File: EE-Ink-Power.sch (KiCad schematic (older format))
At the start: 64 parts, among them J2 USB_A, Q1 IRLML6402, Q2 IRLML6402, Q3 IRLML6402, U4 LM358, U6 MCP73831, U7 MCP1802, U8 LT1945, U9 LT1945

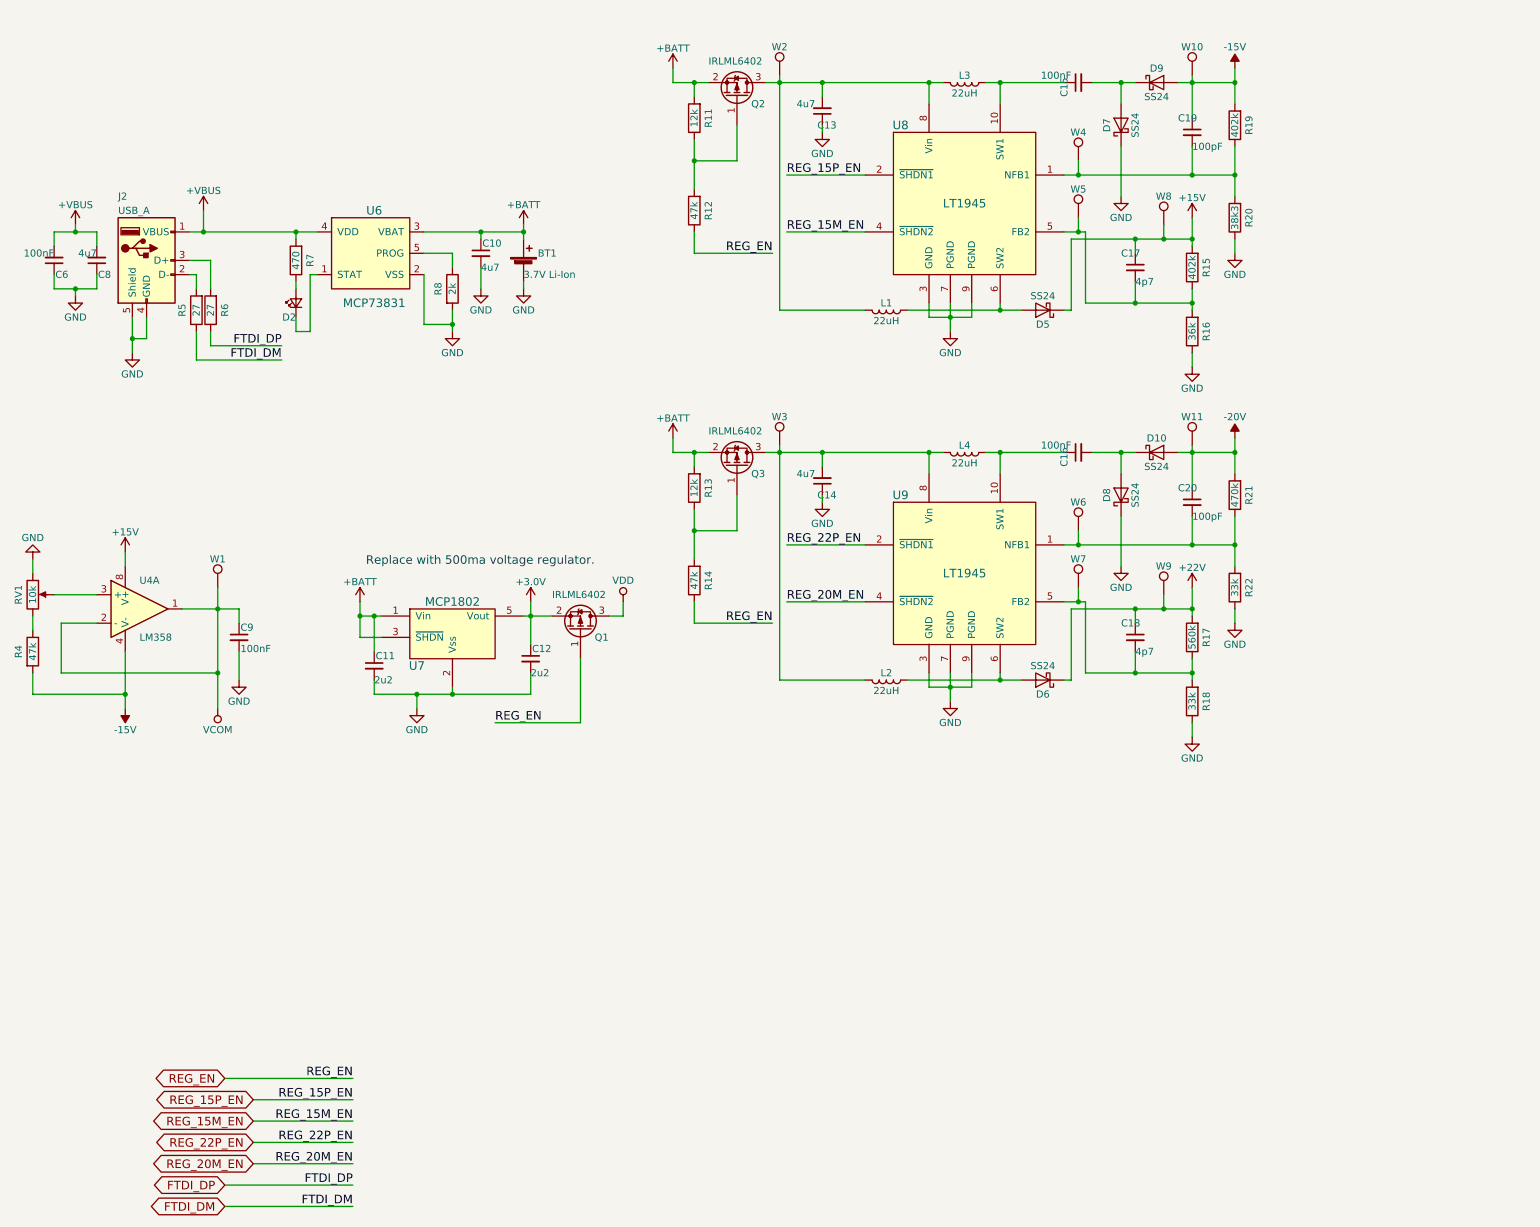
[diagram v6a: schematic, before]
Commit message: Switched out the regulator for a 500ma one.  Cleaned up a few things.
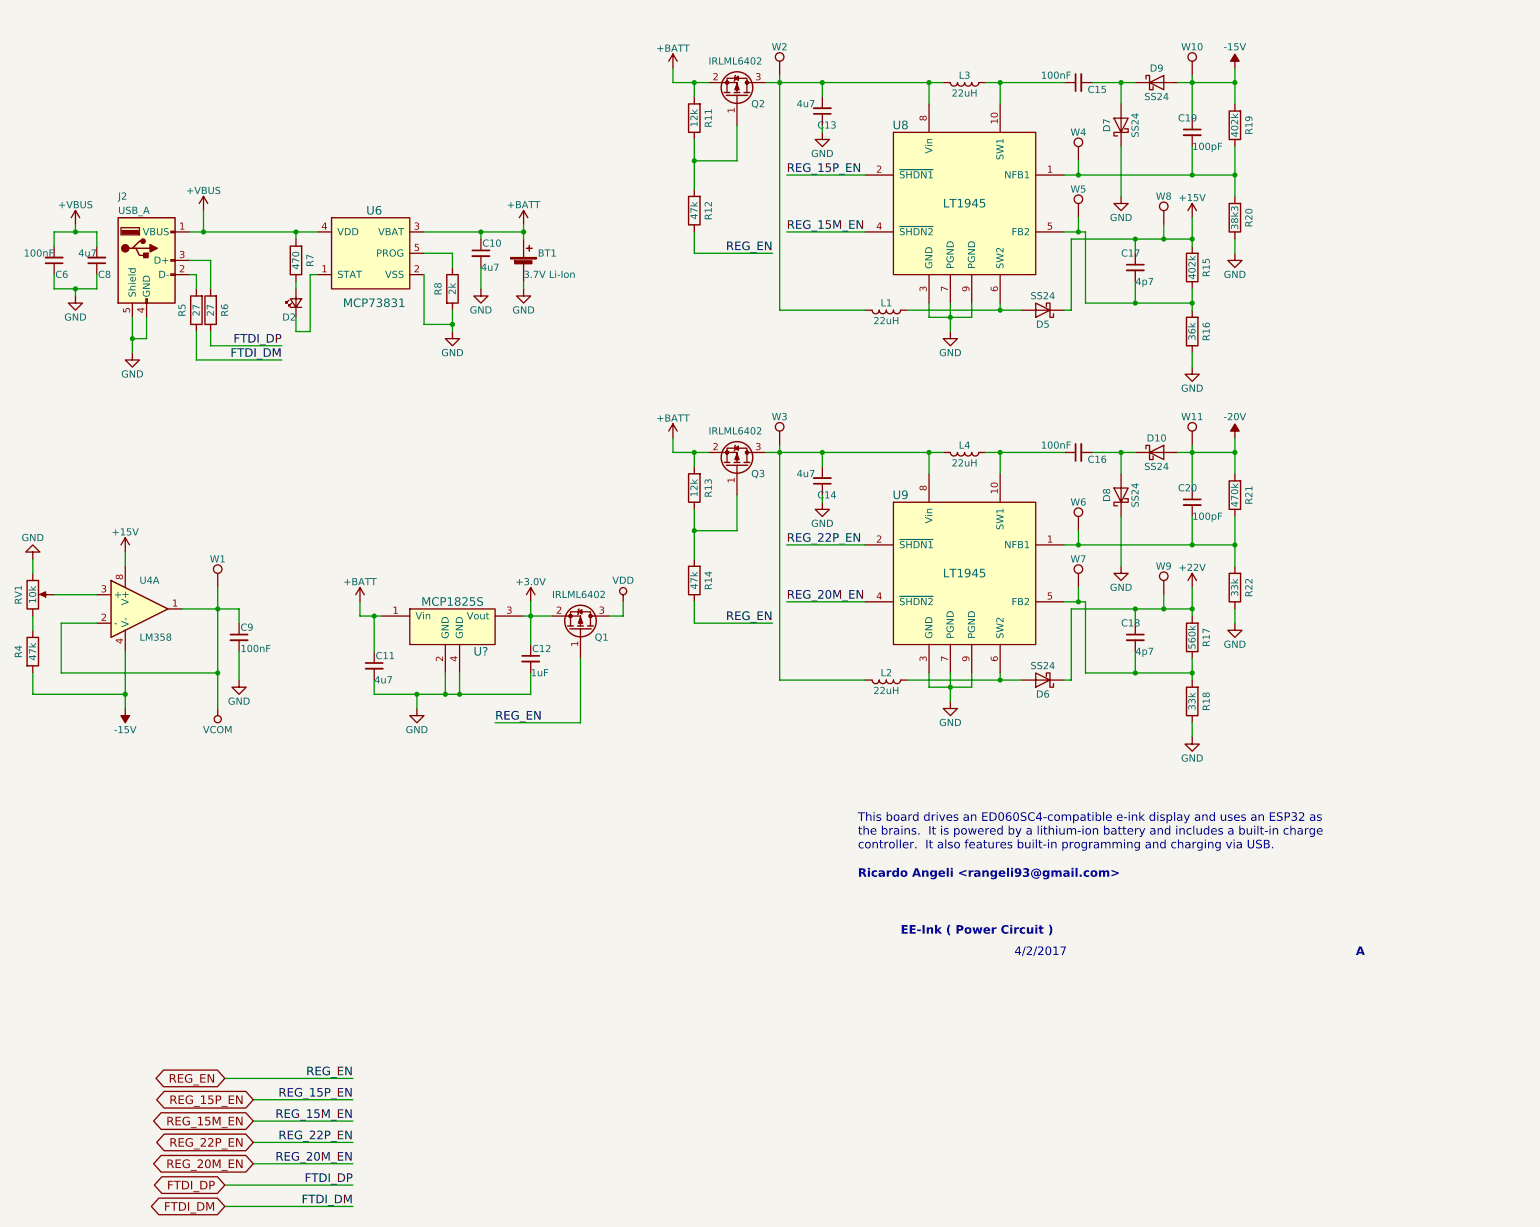
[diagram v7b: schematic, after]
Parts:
- removed U7: MCP1802, symbol MCP1802
- added U?: MCP1825S, symbol MCP1825S
- C11: value 2u2 -> 4u7
- C12: value 2u2 -> 1uF
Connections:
- net +3.0V: now also U?.3 (Vout)
- net +BATT: now also U?.1 (Vin)
- net GND: now also U?.2 (GND), U?.4 (GND)
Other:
- note added: "4/2/2017"
- note added: "A"
- note added: "EE-Ink ( Power Circuit )"
- note added: "Ricardo Angeli <rangeli93@gmail.com>"
- note added: "This board drives an ED060SC4-compatible e-ink display and uses an ESP32 as\nthe brains. It is powered by a lithium-ion battery and includes a built-in charge\ncontroller. It also features built-in programming and charging via USB."
- note removed: "Replace with 500ma voltage regulator."
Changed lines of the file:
@@
 U 1 1 58F29CEA
 P 8600 1500
-F 0 "C15" H 8500 1600 50  0000 L CNN
+F 0 "C15" V 8550 1300 50  0000 L CNN
 F 1 "100nF" V 8650 1550 50  0000 L CNN
 F 2 "" H 8600 1500 50  0001 C CNN
@@
 U 1 1 58F29DC6
 P 8600 4100
-F 0 "C16" H 8500 4200 50  0000 L CNN
+F 0 "C16" V 8550 3900 50  0000 L CNN
 F 1 "100nF" V 8650 4150 50  0000 L CNN
 F 2 "" H 8600 4100 50  0001 C CNN
@@
 $EndComp
 $Comp
-L MCP1802 U7
-U 1 1 58F2D150
-P 4200 5350
-F 0 "U7" H 3950 5100 60  0000 C CNN
-F 1 "MCP1802" H 4200 5550 60  0000 C CNN
-F 2 "" H 4200 5650 60  0001 C CNN
-F 3 "" H 4200 5650 60  0001 C CNN
-	1    4200 5350
-	1    0    0    -1
-$EndComp
-$Comp
 L C_Small C11
 U 1 1 58F2D157
 P 3650 5600
 F 0 "C11" H 3660 5670 50  0000 L CNN
-F 1 "2u2" H 3650 5500 50  0000 L CNN
+F 1 "4u7" H 3650 5500 50  0000 L CNN
 F 2 "" H 3650 5600 50  0001 C CNN
 F 3 "" H 3650 5600 50  0001 C CNN
@@
 $EndComp
 Wire Wire Line
-	3700 5400 3550 5400
-Wire Wire Line
-	3550 5400 3550 5150
-Wire Wire Line
-	3700 5250 3550 5250
-Connection ~ 3550 5250
-Wire Wire Line
-	4200 5800 4200 5750
-Wire Wire Line
 	3650 5800 4750 5800
 Wire Wire Line
@@
 Wire Wire Line
 	3650 5500 3650 5250
-Connection ~ 3650 5250
 $Comp
 L C_Small C12
@@
 P 4750 5550
 F 0 "C12" H 4760 5620 50  0000 L CNN
-F 1 "2u2" H 4750 5450 50  0000 L CNN
+F 1 "1uF" H 4750 5450 50  0000 L CNN
 F 2 "" H 4750 5550 50  0001 C CNN
 F 3 "" H 4750 5550 50  0001 C CNN
@@
 	4750 5150 4750 5450
 Wire Wire Line
-	4700 5250 4900 5250
-Wire Wire Line
 	4750 5800 4750 5650
-Connection ~ 4200 5800
-Connection ~ 4750 5250
 $Comp
 L VDD #PWR040
@@
 Text GLabel 2600 9250 0    60   BiDi ~ 0
 FTDI_DP
-Text Notes 5200 4900 2    60   ~ 0
-Replace with 500ma voltage regulator.
+$Comp
+L MCP1825S U?
+U 1 1 58E808DC
+P 4200 5250
+F 0 "U?" H 4400 5000 60  0000 C CNN
+F 1 "MCP1825S" H 4200 5350 60  0000 C CNN
+F 2 "" H 4100 5200 60  0001 C CNN
+F 3 "" H 4100 5200 60  0001 C CNN
+	1    4200 5250
+	1    0    0    -1
+$EndComp
+Wire Wire Line
+	3550 5250 3700 5250
+Connection ~ 3650 5250
+Wire Wire Line
+	3550 5250 3550 5150
+Wire Wire Line
+	4700 5250 4900 5250
+Connection ~ 4750 5250
+Wire Wire Line
+	4150 5650 4150 5800
+Connection ~ 4150 5800
+Wire Wire Line
+	4250 5650 4250 5800
+Connection ~ 4250 5800
+Text Notes 7350 7500 0    60   ~ 12
+EE-Ink ( Power Circuit )
+Text Notes 7050 6900 0    60   ~ 0
+This board drives an ED060SC4-compatible e-ink display and uses an ESP32 as\nthe brains.  It is powered by a lithium-ion battery and includes a built-in charge\ncontroller.  It also features built-in programming and charging via USB.
+Text Notes 7050 7100 0    60   ~ 12
+Ricardo Angeli <rangeli93@gmail.com>
+Text Notes 8150 7650 0    60   ~ 0
+4/2/2017
+Text Notes 10550 7650 0    60   ~ 12
+A
 $EndSCHEMATC

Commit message: Finished reviewing schematic.  Re-annotated all components.
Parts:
- R15: renamed from R4; value 47k -> 200k
- RV1: value 10k -> 100k
- gave numbers to parts that had none: 1
- renumbered C12 to C11, C13 to C12, C14 to C13, C15 to C14, C16 to C15, C17 to C16, C18 to C17, C19 to C18, C20 to C19, C8 to C7, C9 to C8, C11 to C9, D2 to D4, J2 to J1, Q1 to Q4, Q2 to Q5, Q3 to Q6, R5 to R16, R6 to R17, R7 to R18, R8 to R19, R11 to R20, R12 to R21, R13 to R22, R14 to R23, R15 to R24, R16 to R25, R17 to R26, R18 to R27, R19 to R28, R20 to R29, R21 to R30, R22 to R31, U4 to U5
